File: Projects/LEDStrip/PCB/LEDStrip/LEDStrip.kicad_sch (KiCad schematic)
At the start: 33 parts, among them J1 USB_C_Receptacle_USB2.0_14P, U1 MSGEQ7, U2 ESP32-S3-WROOM-1, U3 LM2596S-5, U4 AMS1117-3.3

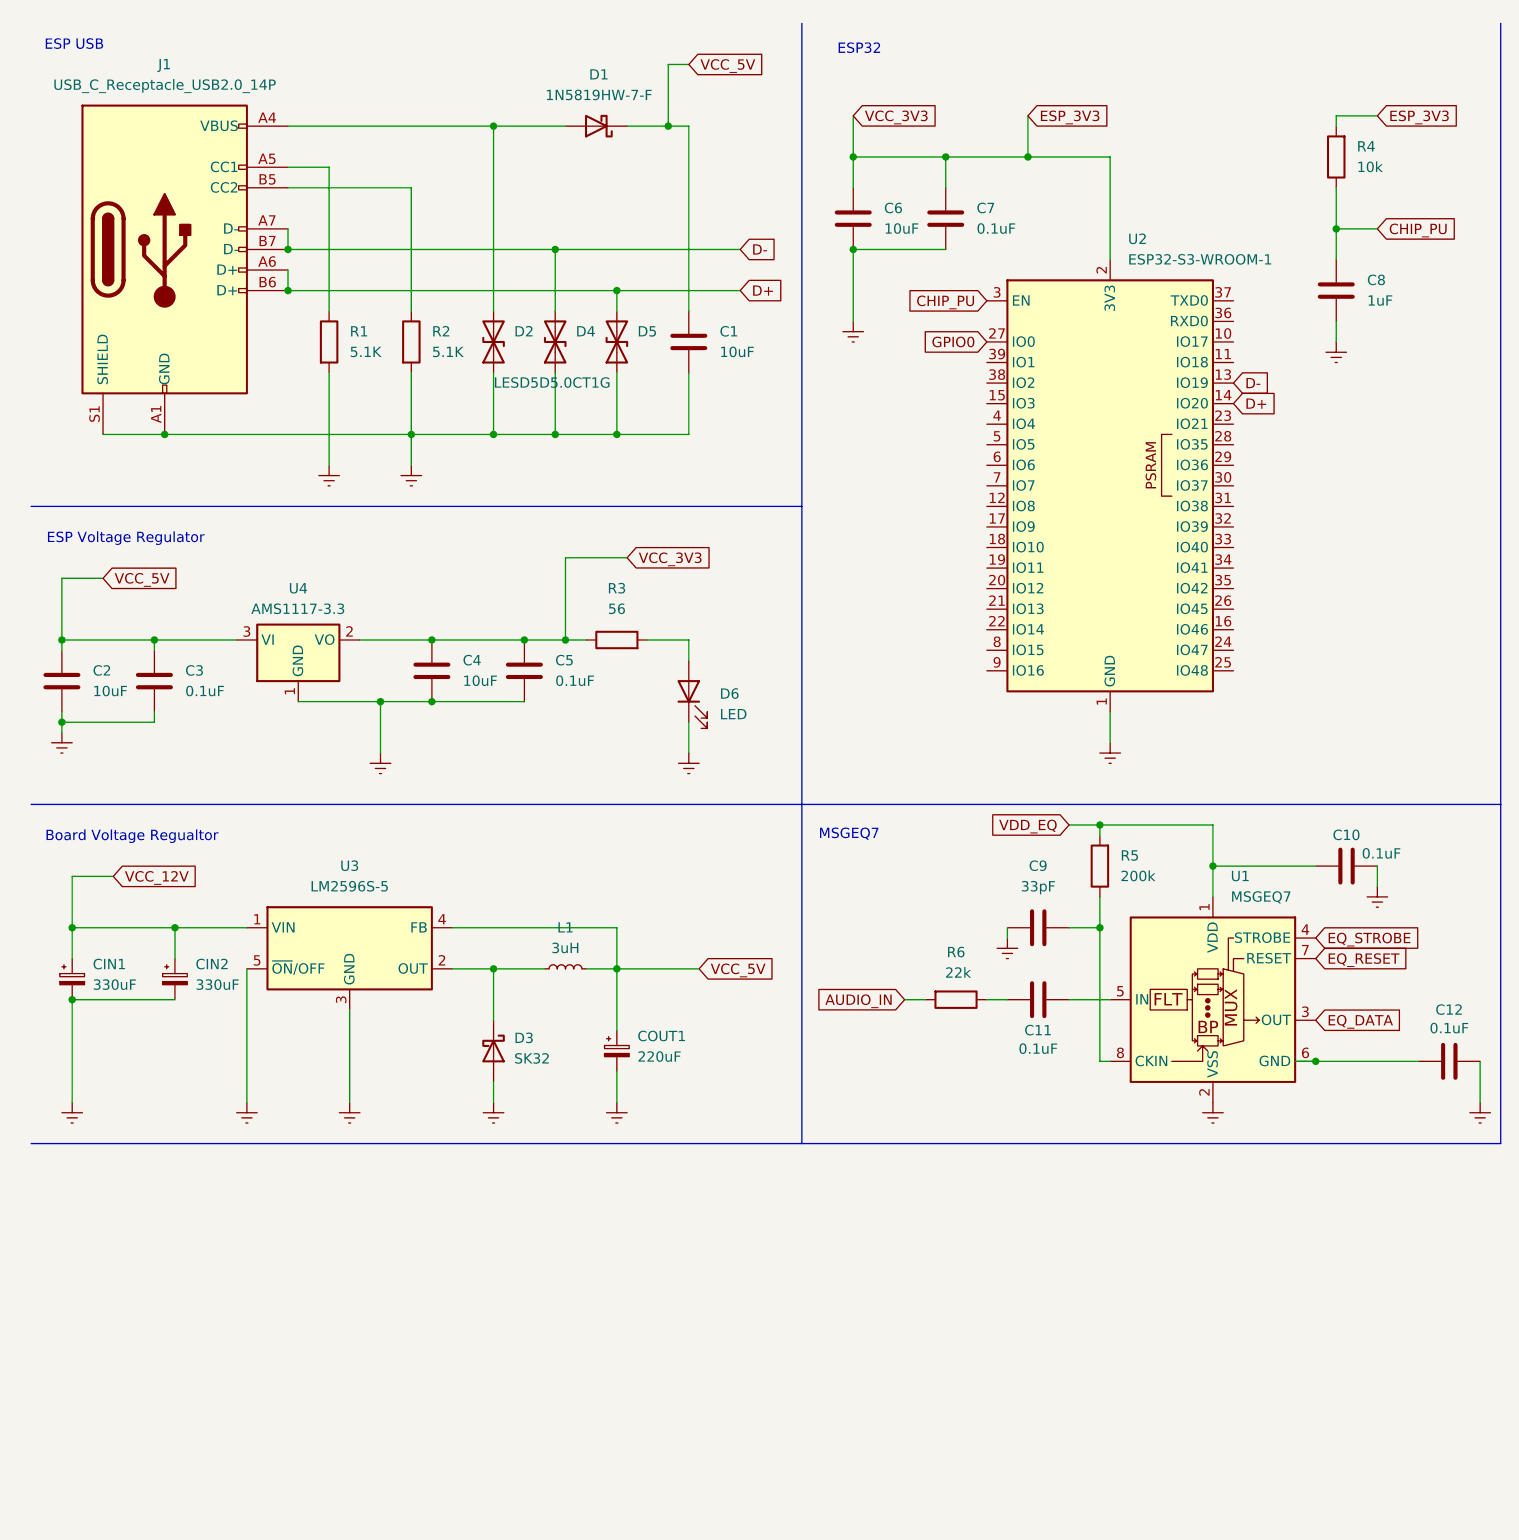
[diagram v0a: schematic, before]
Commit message: core esp32 sections complete
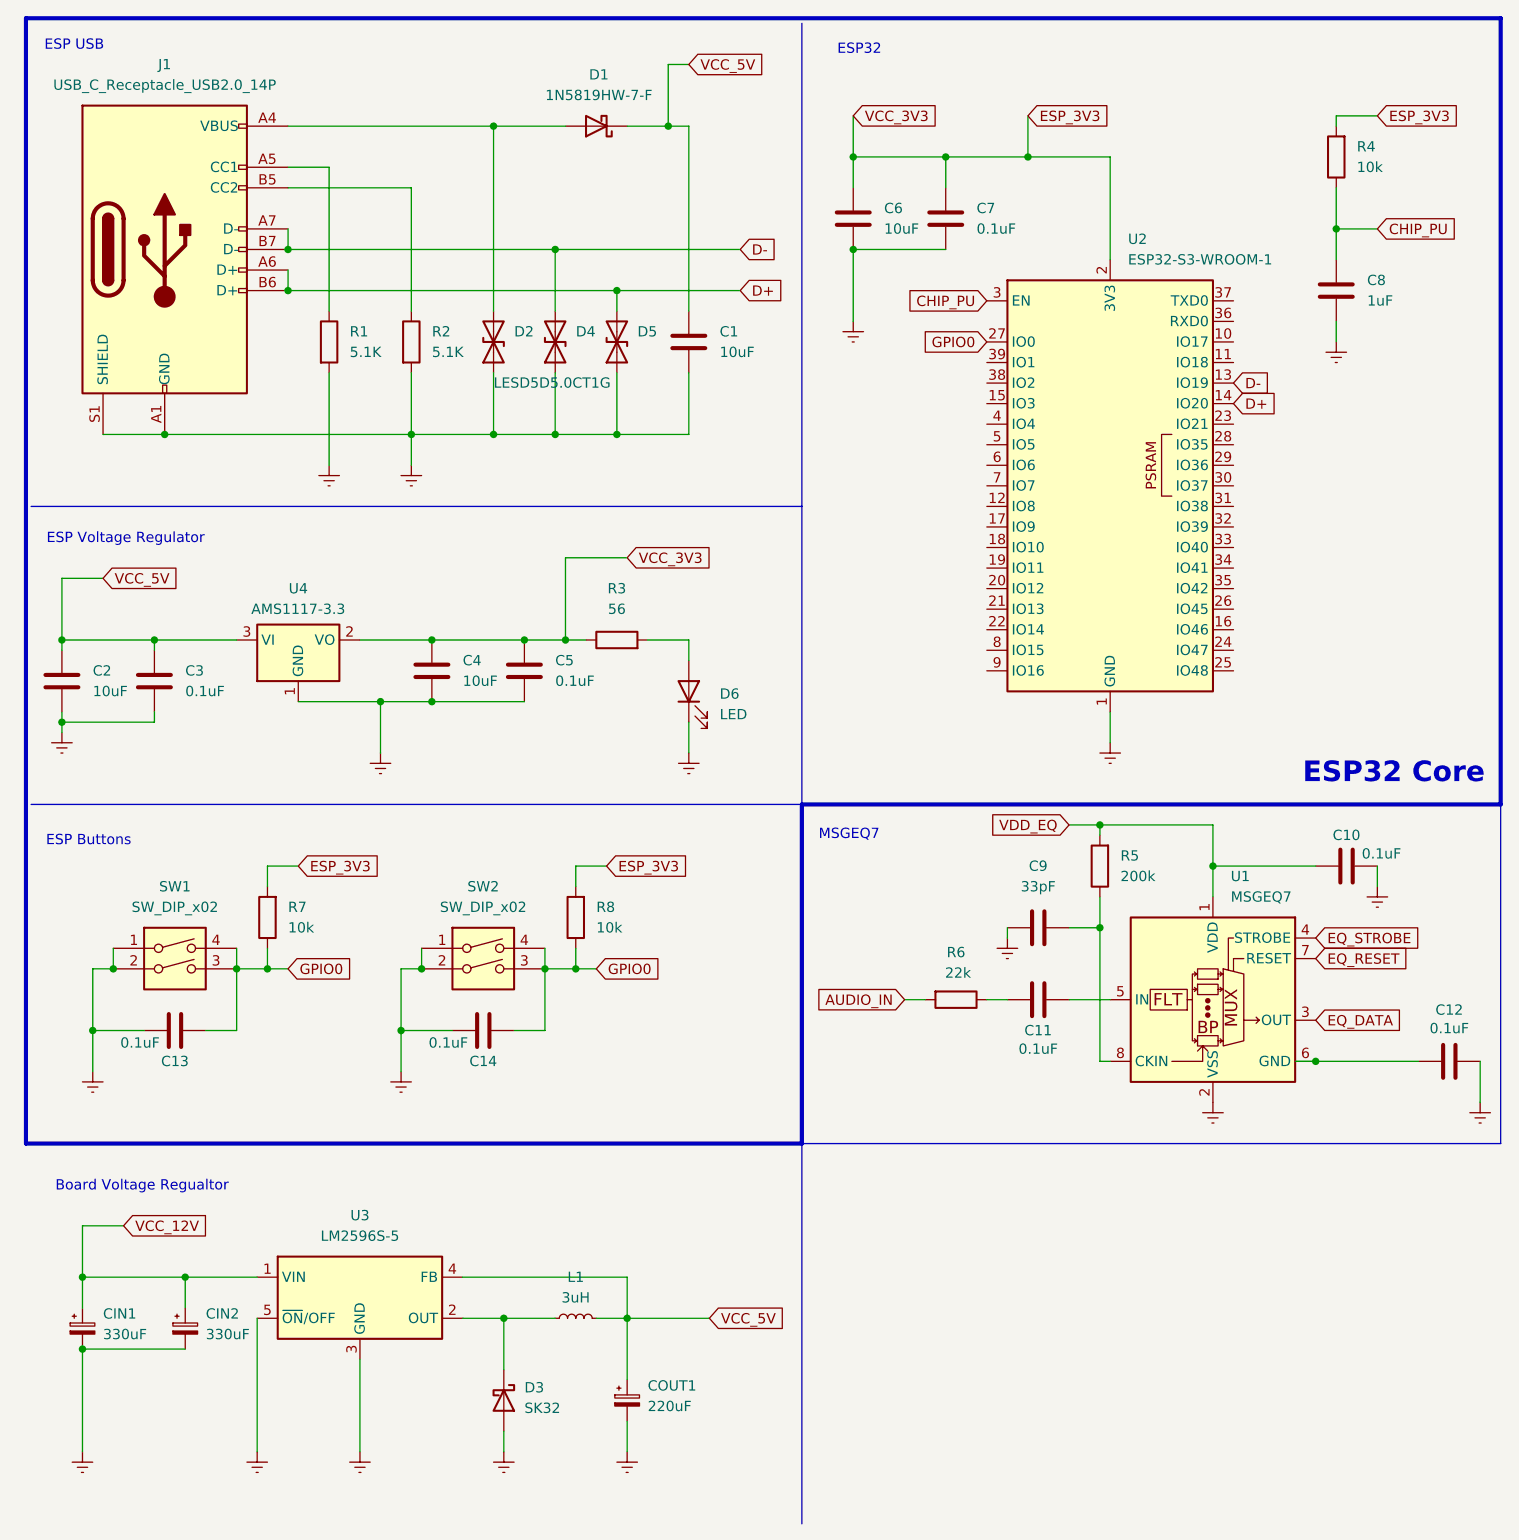
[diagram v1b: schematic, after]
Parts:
- added C13, C14: 0.1uF, Capacitor_SMD:C_0603_1608Metric, symbol Device:C
- added R7, R8: 10k, Resistor_SMD:R_0603_1608Metric, symbol Device:R
- added SW1, SW2: SW_DIP_x02, Button_Switch_SMD:SW_Push_1P1T_NO_CK_KMR2, symbol Switch:SW_DIP_x02
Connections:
- net ESP_3V3: now also R7.2, R8.2
- net GPIO0: now also C13.1, C14.1, R7.1, R8.1, SW1.3, SW1.4, SW2.3, SW2.4
- new net: C14.2, SW2.1, SW2.2
- new net: C13.2, SW1.1, SW1.2
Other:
- note added: "ESP Buttons"
- note added: "ESP32 Core"
- moved on the sheet: CIN1, CIN2, COUT1, D3, L1, U3
